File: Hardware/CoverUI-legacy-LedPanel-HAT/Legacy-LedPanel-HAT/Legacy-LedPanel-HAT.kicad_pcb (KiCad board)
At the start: 2 copper layers, 100 x 90.1 mm, 37 parts, among them J1 Conn_02x20_Odd_Even, J10 2mm, J11 2.54mm, J12 Spare LevelShift A0_A1, J13 Spare LS OUT B0_B1, J14 LS OUT S1_S2, J16 I2C, J2 OM_Serial, J3 1.8mm, J4 2mm, J5 SOUT_to_STM32, J5_STOP1 2.54mm, J6_STOP2 2.54mm, J7 2mm, J8 1.8mm, J9 1.8mm, U1 STM32F401RC blue pill, U2 74LVC4245AD, U3 STM32F401RC blue pill, U4 LSF0108PWJ, U5 LSF0108PWJ, U6 LSF0108PWJ, U7 LSF0108PWJ, U8 STM32F401RC blue pill

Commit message: commit before merge
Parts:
- removed J9: 1.8mm, CustomFootprintLibrary:conn_01x9_1.8mm
- removed JP15: LS GND_or_5V, Connector_PinHeader_2.54mm:PinHeader_1x03_P2.54mm_Vertical
- added C1: 0.1uF, Capacitor_SMD:C_1206_3216Metric_Pad1.33x1.80mm_HandSolder, F.Cu at (75.3, 110.9)
- added J6: 3V3 out, Connector_PinHeader_2.54mm:PinHeader_1x03_P2.54mm_Vertical, F.Cu at (144.5, 99.0)
- added R1: 200k, Resistor_SMD:R_1206_3216Metric_Pad1.30x1.75mm_HandSolder, F.Cu at (75.3, 113.8)
- J10: footprint Connector_JST:JST_PH_S9B-PH-K_1x09_P2.00mm_Horizontal -> Connector_JST:JST_PH_B9B-PH-K_1x09_P2.00mm_Vertical
- J11: footprint Connector_JST:JST_XH_S9B-XH-A-1_1x09_P2.50mm_Horizontal -> Connector_JST:JST_XH_B9B-XH-A_1x09_P2.50mm_Vertical
- J12: value Spare LevelShift A0_A1 -> Spare LevelShift A6-8; footprint Connector_PinHeader_2.54mm:PinHeader_1x02_P2.54mm_Horizontal -> Connector_PinHeader_2.54mm:PinHeader_1x03_P2.54mm_Vertical; moved to F.Cu
- J13: value Spare LS OUT B0_B1 -> Spare LS OUT B6-8; footprint Connector_PinHeader_2.54mm:PinHeader_1x02_P2.54mm_Horizontal -> Connector_PinHeader_2.54mm:PinHeader_1x03_P2.54mm_Vertical
- J14: value LS OUT S1_S2 -> LS OUT S1_S2_SOUT; footprint Connector_PinHeader_2.54mm:PinHeader_1x02_P2.54mm_Horizontal -> Connector_PinHeader_2.54mm:PinHeader_1x03_P2.54mm_Vertical
- J16: footprint Connector_PinHeader_2.54mm:PinHeader_1x02_P2.54mm_Horizontal -> Connector_PinHeader_2.54mm:PinHeader_1x02_P2.54mm_Vertical
- J3: value 1.8mm -> Pill Widening; footprint CustomFootprintLibrary:conn_01x2_1.8mm -> Connector_PinHeader_2.54mm:PinHeader_1x20_P2.54mm_Vertical
- J5: value SOUT_to_STM32 -> 5V out; footprint Connector_PinHeader_2.54mm:PinHeader_1x02_P2.54mm_Vertical -> Connector_PinHeader_2.54mm:PinHeader_1x03_P2.54mm_Vertical
- J8: value 1.8mm -> GND out; footprint CustomFootprintLibrary:conn_01x2_1.8mm -> Connector_PinHeader_2.54mm:PinHeader_1x03_P2.54mm_Vertical
- JP7: value STOP1 GND_or_5V -> ESTOP 5V_or_3V3
- JP8: value STOP2 GND_or_5V -> ESTOP1 LS_or_uC
- U1: footprint STM32 Pills:YAAJ_BluePill_SWD_1 -> stm32_pills:YAAJ_WeAct_BlackPill_SWD_2
- U2: value 74LVC4245AD -> LSF0108PWJ; footprint NXP 74LVC4245AD:SOT137-1_NEX -> lsf0108_level_shifter:TSSOP20_SOT360-1_NEX
- U4, U5, U6, U7: footprint footprints:TSSOP20_SOT360-1_NEX -> lsf0108_level_shifter:TSSOP20_SOT360-1_NEX
- moved JP8 80.3 mm to (54.1, 125.8)
- moved J7 72.1 mm to (53.1, 120.8), turned to 90 degrees
- moved J6_STOP2 69.0 mm to (55.3, 120.9), turned to 90 degrees
- moved J5 68.5 mm to (135.7, 99.0), turned to 0 degrees
- moved J4 68.2 mm to (53.1, 133.2), turned to 90 degrees
- moved J5_STOP1 64.8 mm to (55.4, 133.4), turned to 90 degrees
- moved J10 37.3 mm to (56.3, 98.6), turned to 0 degrees
- moved J11 35.2 mm to (53.8, 101.6), turned to 0 degrees
- moved JP7 23.7 mm to (84.0, 98.6), turned to 90 degrees
- moved J3 21.1 mm to (96.2, 109.6)
- moved J8 16.7 mm to (140.2, 99.0), turned to 0 degrees
- moved J13 14.9 mm to (84.0, 113.0), turned to -90 degrees
- moved J12 12.6 mm to (59.7, 112.3), turned to -90 degrees
- moved J16 10.9 mm to (129.3, 102.2), turned to -90 degrees
- moved JP1 4.69 mm to (85.5, 129.9)
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- renumbered C1 to C2, C2 to C3, C3 to C4, C4 to C5, R1 to R2, R2 to R3, R3 to R4, R4 to R5
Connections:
- J14 pad 1: /S1_LS -> /S2_LS
- J14 pad 2: /S2_LS -> /S1_LS
- J16 pad 1: /JP1-10 LiftX -> /SCL1
- J16 pad 2: Net-(J16-Pin_2) -> /SDA1
- J3 pad 1: Net-(J3-Pin_1) -> /ESTOP
- J3 pad 2: /JP6-2 STOP2 -> /JP1-1 Right Bumper
- J4 pad 1: Net-(J3-Pin_1) -> Net-(J4-Pin_1)
- J4 pad 2: /JP6-2 STOP2 -> Net-(J4-Pin_2)
- J5 pad 1: /SOUT_LS -> +5V
- J5 pad 2: /JP1-10 LiftX -> +5V
- J5_STOP1 pad 1: Net-(J3-Pin_1) -> Net-(J4-Pin_1)
- J5_STOP1 pad 2: /JP6-2 STOP2 -> Net-(J4-Pin_2)
- J6_STOP2 pad 1: Net-(J6_STOP2-Pin_1) -> Net-(J4-Pin_2)
- J6_STOP2 pad 2: /JP5-2 STOP1 -> /ESTOP1_5V
- J7 pad 1: Net-(J6_STOP2-Pin_1) -> Net-(J4-Pin_2)
- J7 pad 2: /JP5-2 STOP1 -> /ESTOP1_5V
- J8 pad 1: Net-(J6_STOP2-Pin_1) -> GND
- J8 pad 2: /JP5-2 STOP1 -> GND
- JP1 pad 1: Net-(JP1-A) -> /3V3
- JP1 pad 3: Net-(JP1-B) -> +5V
- JP2 pad 1: Net-(JP1-B) -> +5V
- JP2 pad 3: Net-(JP2-B) -> /3V3
- JP7 pad 1: GND -> +5V
- JP7 pad 2: Net-(J3-Pin_1) -> /ESTOP2_5V
- JP7 pad 3: +5V -> /3V3
- JP8 pad 1: GND -> /ESTOP_5V
- JP8 pad 2: Net-(J6_STOP2-Pin_1) -> Net-(J4-Pin_1)
- JP8 pad 3: +5V -> /ESTOP
- U1 pad 1: /ESTOP1 -> /ESTOP
- U1 pad 14: /JP1-10 LiftX -> /SCL1
- U1 pad 15: Net-(J16-Pin_2) -> /SDA1
- U1 pad 2: /ESTOP2 -> /JP1-1 Right Bumper
- U1 pad 20: Net-(JP2-B) -> /3V3
- U1 pad 3: /JP1-1 Right Bumper -> /JP1-4 Lift
- U1 pad 38: Net-(JP1-A) -> /3V3
- U1 pad 4: /JP1-4 Lift -> /JP6-2 STOP2
- U1 pad 40: Net-(JP1-B) -> +5V
- U1 pad 5: /JP6-2 STOP2 -> /JP1-7 Left Bumper
- U1 pad 6: /JP1-7 Left Bumper -> /JP1-10 LiftX
- U2 pad 1: +5V -> GND
- U2 pad 10: /SOUT_5V -> Net-(J12-Pin_3)
- U2 pad 11: GND -> Net-(J13-Pin_3)
- U2 pad 12: GND -> Net-(J13-Pin_2)
- U2 pad 13: GND -> Net-(J13-Pin_1)
- U2 pad 18: /ESTOP1 -> /ESTOP
- U2 pad 19: /ESTOP2 -> Net-(U2-EN)
- U2 pad 2: Net-(JP15-C) -> +5V
- U2 pad 20: Net-(J13-Pin_2) -> Net-(U2-EN)
- U2 pad 3: Net-(J12-Pin_1) -> /ESTOP_5V
- U2 pad 4: Net-(J12-Pin_2) -> /RAIN_5V
- U2 pad 5: /ESTOP2_5V -> /S2_5V
- U2 pad 6: /ESTOP1_5V -> /S1_5V
- U2 pad 7: /RAIN_5V -> /SOUT_5V
- U2 pad 8: /S2_5V -> Net-(J12-Pin_1)
- U2 pad 9: /S1_5V -> Net-(J12-Pin_2)
- U3 pad 18: Net-(U4-REFA) -> +5V
- U3 pad 40: Net-(U4-REFA) -> +5V
- U4 pad 2: Net-(U4-REFA) -> +5V
- U5 pad 2: Net-(U4-REFA) -> +5V
- U6 pad 2: Net-(U4-REFA) -> +5V
- U7 pad 2: Net-(U4-REFA) -> +5V
- U8 pad 18: Net-(U4-REFA) -> +5V
- U8 pad 40: Net-(U4-REFA) -> +5V
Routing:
- net /3V3: track 0.00 -> 168.8 mm
- net Net-(U4-REFA): track 149.0 -> 0.00 mm
- net Net-(JP2-B): track 146.5 -> 0.00 mm
- net +5V: track 298.2 -> 434.2 mm
- net /JP1-10 LiftX: track 133.1 -> 60.5 mm
- net /ESTOP: track 0.00 -> 57.6 mm
- net /ESTOP_5V: track 0.00 -> 25.9 mm
- net Net-(J6_STOP2-Pin_1): track 24.1 -> 0.00 mm
- net /JP6-2 STOP2: track 81.7 -> 58.6 mm
- net /ESTOP1_5V: track 21.5 -> 43.6 mm
- net Net-(J16-Pin_2): track 21.4 -> 0.00 mm
- net /JP5-2 STOP1: track 84.2 -> 63.5 mm
- net Net-(J12-Pin_3): track 0.00 -> 20.3 mm
- net Net-(J3-Pin_1): track 20.0 -> 0.00 mm
- net Net-(JP1-A): track 19.6 -> 0.00 mm
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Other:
- outline, holes or cut-outs redrawn
- board text added: "BOTTOM (uC) - facing CoverUI"
- board text added: "CoverUI Legacy LED Hat Design by Tamas Dajka OpenMower project v0.2"
- board text added: "J7"
- board text added: "TOP"
- board text removed: "CoverUI Legacy LED Hat Design by Tamas Dajka OpenMower project"

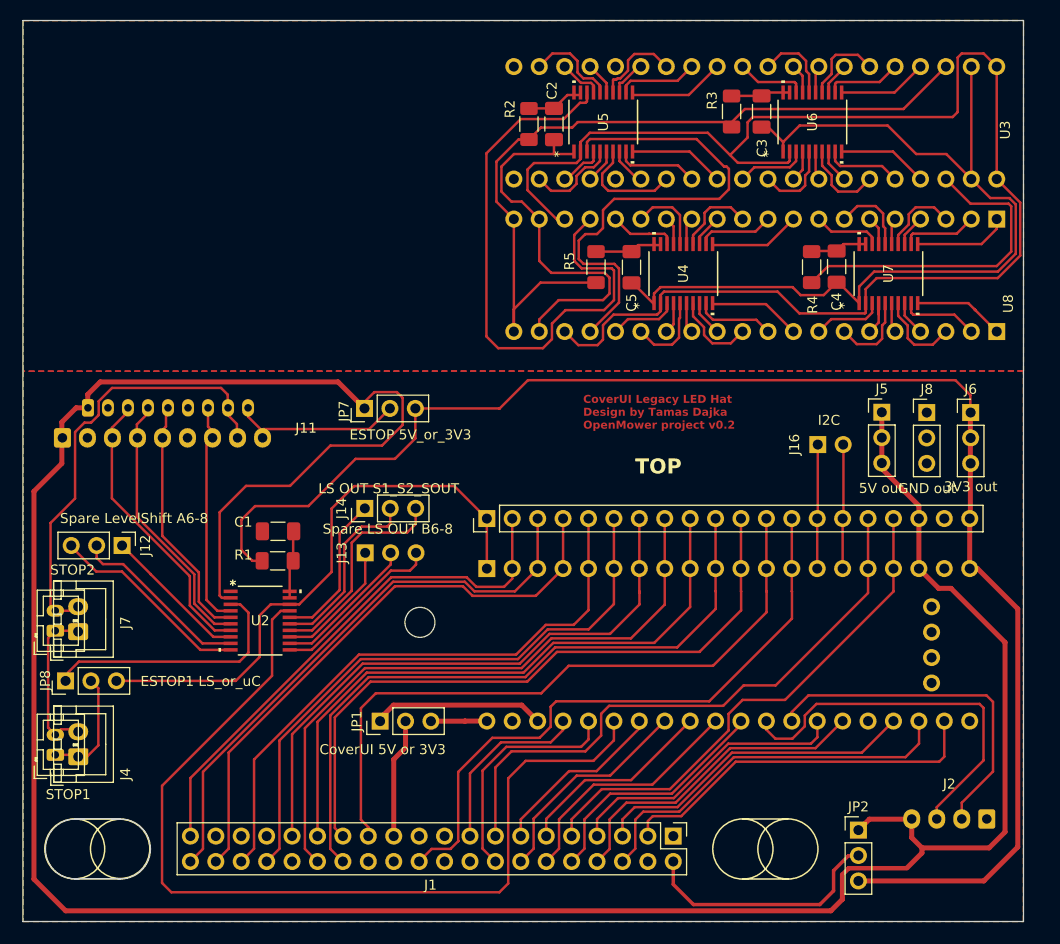
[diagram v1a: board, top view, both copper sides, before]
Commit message: HW redesign based on first live tests (new design not tested)
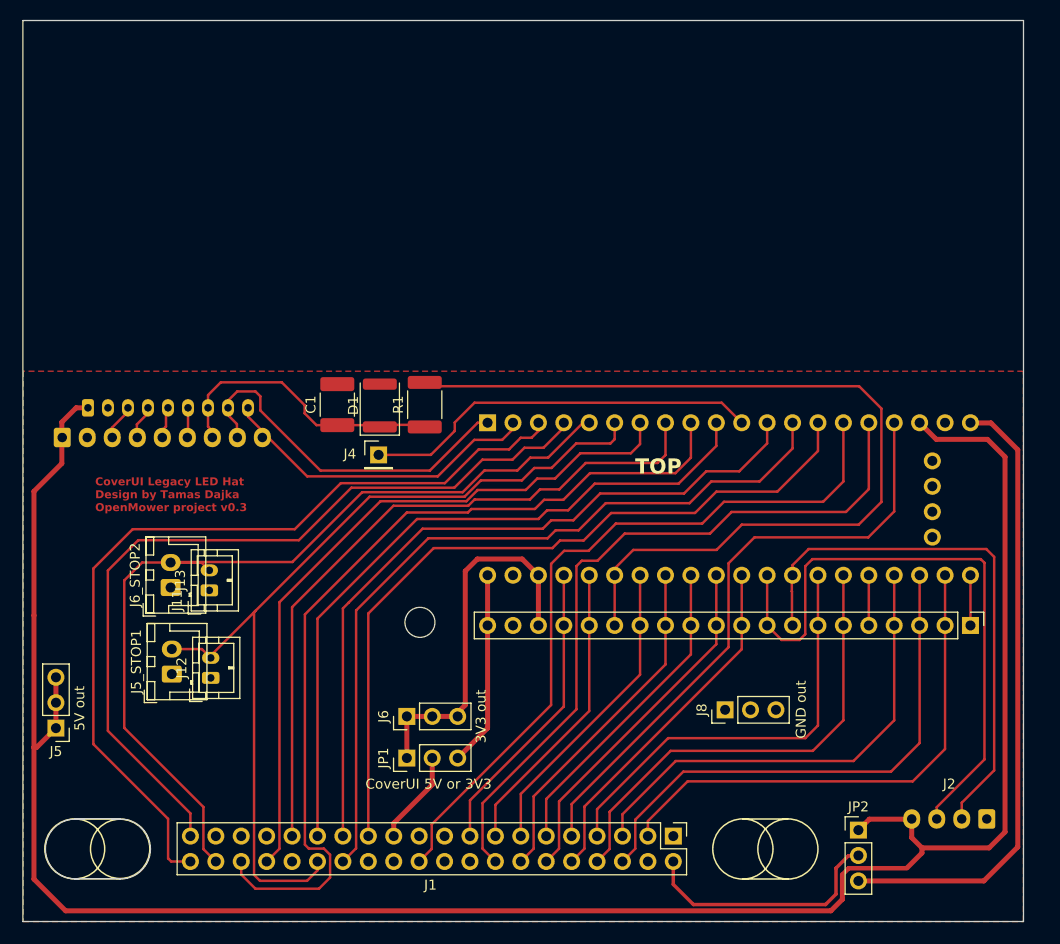
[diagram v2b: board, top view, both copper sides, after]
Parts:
- removed C2, C3, C4, C5: 0.1uF, Capacitor_SMD:C_1206_3216Metric_Pad1.33x1.80mm_HandSolder
- removed J14: LS OUT S1_S2_SOUT, Connector_PinHeader_2.54mm:PinHeader_1x03_P2.54mm_Vertical
- removed J16: I2C, Connector_PinHeader_2.54mm:PinHeader_1x02_P2.54mm_Vertical
- removed J7: 2mm, Connector_JST:JST_PH_B2B-PH-K_1x02_P2.00mm_Vertical
- removed JP7: ESTOP 5V_or_3V3, Connector_PinHeader_2.54mm:PinHeader_1x03_P2.54mm_Vertical
- removed JP8: ESTOP1 LS_or_uC, Connector_PinHeader_2.54mm:PinHeader_1x03_P2.54mm_Vertical
- removed R2, R3, R4, R5: 200k, Resistor_SMD:R_1206_3216Metric_Pad1.30x1.75mm_HandSolder
- removed U2, U4, U5, U6, U7: LSF0108PWJ, lsf0108_level_shifter:TSSOP20_SOT360-1_NEX
- removed U3, U8: STM32F401RC blue pill, STM32 Pills:YAAJ_BluePill_1
- added D1: PDZ3.3B.115, Diode_SMD:D_1812_4532Metric, F.Cu at (85.5, 98.3)
- C1: value 0.1uF -> 100nF; footprint Capacitor_SMD:C_1206_3216Metric_Pad1.33x1.80mm_HandSolder -> Capacitor_SMD:C_1812_4532Metric
- J12: value Spare LevelShift A6-8 -> 2mm; footprint Connector_PinHeader_2.54mm:PinHeader_1x03_P2.54mm_Vertical -> Connector_JST:JST_PH_B2B-PH-K_1x02_P2.00mm_Vertical
- J13: value Spare LS OUT B6-8 -> 2mm; footprint Connector_PinHeader_2.54mm:PinHeader_1x03_P2.54mm_Vertical -> Connector_JST:JST_PH_B2B-PH-K_1x02_P2.00mm_Vertical; moved to F.Cu
- J4: value 2mm -> SWO; footprint Connector_JST:JST_PH_B2B-PH-K_1x02_P2.00mm_Vertical -> Connector_PinHeader_2.54mm:PinHeader_1x01_P2.54mm_Vertical
- R1: value 200k -> 10k; footprint Resistor_SMD:R_1206_3216Metric_Pad1.30x1.75mm_HandSolder -> Resistor_SMD:R_1812_4532Metric_Pad1.30x3.40mm_HandSolder
- moved J5 88.4 mm to (53.1, 130.6), turned to 180 degrees
- moved J6 64.0 mm to (88.2, 129.4), turned to 90 degrees
- moved J3 49.5 mm to (144.5, 120.3), turned to -90 degrees
- moved J4 44.1 mm to (85.4, 103.3), turned to 0 degrees
- moved J8 35.9 mm to (120.0, 128.7), turned to 90 degrees
- moved R1 21.4 mm to (90.0, 98.2), turned to 90 degrees
- moved J13 16.0 mm to (68.5, 116.8), turned to 90 degrees
- moved J12 15.9 mm to (68.6, 125.5), turned to 90 degrees
- moved U1 14.6 mm to (96.3, 100.0)
- moved C1 14.0 mm to (81.2, 98.2), turned to 90 degrees
- moved J5_STOP1 12.5 mm to (64.7, 125.2)
- moved J6_STOP2 10.2 mm to (64.6, 116.5)
- moved JP1 4.55 mm to (88.2, 133.6)
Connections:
- C1 pad 1: Net-(U2-EN) -> /RAIN_5V
- J1 pad 17: /LED11 - D11 -> /LED11 - D11 (S2 LED)
- J10 pad 6: GND -> /GAIN
- J10 pad 8: /ESTOP1_5V -> /ESTOP1
- J10 pad 9: /ESTOP2_5V -> /ESTOP2
- J11 pad 6: GND -> /GAIN
- J11 pad 8: /ESTOP1_5V -> /ESTOP1
- J11 pad 9: /ESTOP2_5V -> /ESTOP2
- J12 pad 1: Net-(J12-Pin_1) -> GND
- J12 pad 2: Net-(J12-Pin_2) -> /JP5-2 STOP1
- J13 pad 1: Net-(J13-Pin_1) -> GND
- J13 pad 2: Net-(J13-Pin_2) -> /JP6-2 STOP2
- J3 pad 1: /ESTOP -> Net-(J3-Pin_1)
- J3 pad 10: /S8 (button) -> /LED6 - D6
- J3 pad 11: /S9 (button) -> /LED7 - D7
- J3 pad 12: /S7 (button) -> /S3 (button)
- J3 pad 13: /S1 (button) -> /LED8 - D8
- J3 pad 14: /SCL1 -> /S5 (button)
- J3 pad 15: /SDA1 -> /RAIN
- J3 pad 17: /S2 (button) -> /LED11 - D11 (S2 LED)
- J3 pad 18: +5V -> /3V3
- J3 pad 2: /JP1-1 Right Bumper -> /LED1 - D1
- J3 pad 20: /3V3 -> +5V
- J3 pad 3: /JP1-4 Lift -> /LED3 - D3
- J3 pad 4: /JP6-2 STOP2 -> /LED2 - D2
- J3 pad 5: /JP1-7 Left Bumper -> Net-(J3-Pin_5)
- J3 pad 6: /JP1-10 LiftX -> /LED5 - D5
- J3 pad 7: /S6 (button) -> /LED4 - D4
- J3 pad 8: /JP5-2 STOP1 -> /Pico-RX_STM32-TX
- J3 pad 9: /S4 (button) -> /Pico-TX_STM32-RX
- J5_STOP1 pad 1: Net-(J4-Pin_1) -> GND
- J5_STOP1 pad 2: Net-(J4-Pin_2) -> /JP5-2 STOP1
- J6_STOP2 pad 1: Net-(J4-Pin_2) -> GND
- J6_STOP2 pad 2: /ESTOP1_5V -> /JP6-2 STOP2
- R1 pad 1: Net-(U2-EN) -> /RAIN_5V
- R1 pad 2: /3V3 -> /RAIN
- U1 pad 1: /ESTOP -> /ESTOP1
- U1 pad 10: /S8 (button) -> /S4 (button)
- U1 pad 11: /S9 (button) -> Net-(J4-Pin_1)
- U1 pad 12: /S7 (button) -> /S9 (button)
- U1 pad 13: /S1 (button) -> /S8 (button)
- U1 pad 14: /SCL1 -> /S7 (button)
- U1 pad 15: /SDA1 -> /S1 (button)
- U1 pad 16: /LED10 - D10 -> /LED9 - D9
- U1 pad 2: /JP1-1 Right Bumper -> /ESTOP2
- U1 pad 21: unconnected-(U1-VBat-Pad21) -> Net-(J3-Pin_1)
- U1 pad 25: unconnected-(U1-RST-Pad25) -> Net-(J3-Pin_5)
- U1 pad 36: /LED9 - D9 -> /LED10 - D10
- U1 pad 37: /LED11 - D11 -> /LED11 - D11 (S2 LED)
- U1 pad 4: /JP6-2 STOP2 -> /JP1-1 Right Bumper
- U1 pad 5: /JP1-7 Left Bumper -> /JP6-2 STOP2
- U1 pad 6: /JP1-10 LiftX -> /JP5-2 STOP1
- U1 pad 7: /S6 (button) -> /JP1-10 LiftX
- U1 pad 8: /JP5-2 STOP1 -> /S6 (button)
- U1 pad 9: /S4 (button) -> /JP1-7 Left Bumper
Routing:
- net +5V: track 434.2 -> 237.4 mm
- net GND: track 132.1 -> 0.00 mm
- net Net-(R2-Pad2): track 112.2 -> 0.00 mm
- net /3V3: track 168.8 -> 99.9 mm
- net Net-(U3-PB9): track 59.4 -> 0.00 mm
- net /ESTOP: track 57.6 -> 0.00 mm
- net Net-(U5-A1): track 50.5 -> 0.00 mm
- net /LED9 - D9: track 23.3 -> 73.0 mm
- net /ESTOP1_5V: track 43.6 -> 0.00 mm
- net /ESTOP1: track 0.00 -> 35.8 mm
- net /ESTOP2: track 0.00 -> 32.7 mm
- net /JP6-2 STOP2: track 58.6 -> 89.2 mm
- net /LED11 - D11 (S2 LED): track 0.00 -> 30.2 mm
- net /LED10 - D10: track 60.1 -> 30.1 mm
- net /JP1-1 Right Bumper: track 53.0 -> 81.9 mm
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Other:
- board text added: "CoverUI Legacy LED Hat Design by Tamas Dajka OpenMower project v0.3"
- board text removed: "CoverUI Legacy LED Hat Design by Tamas Dajka OpenMower project v0.2"
- board text removed: "J7"

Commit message: last version
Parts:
- J10, J11: moved to F.Cu
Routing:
- net GND: track 0.00 -> 130.7 mm
- added copper zone on B.Cu, net GND
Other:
- board size 100 x 90.1 mm -> 100 x 55.3 mm
- board text added: "3V3"
- board text added: "5V"
- board text added: "GND"
- board text added: "SWCLK"
- board text added: "SWDIO"
